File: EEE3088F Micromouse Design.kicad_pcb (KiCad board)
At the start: 2 copper layers, 70 x 78.2 mm, 39 parts, among them J1 Conn_02x16_Odd_Even, J2 Conn_01x02, J3 TYPE-C-31-M-12, SW1 SW_SPDT, U1 INA219AxD, U2 XL1509-3.3, U7 TPS61088RHLR, U9 CH224K

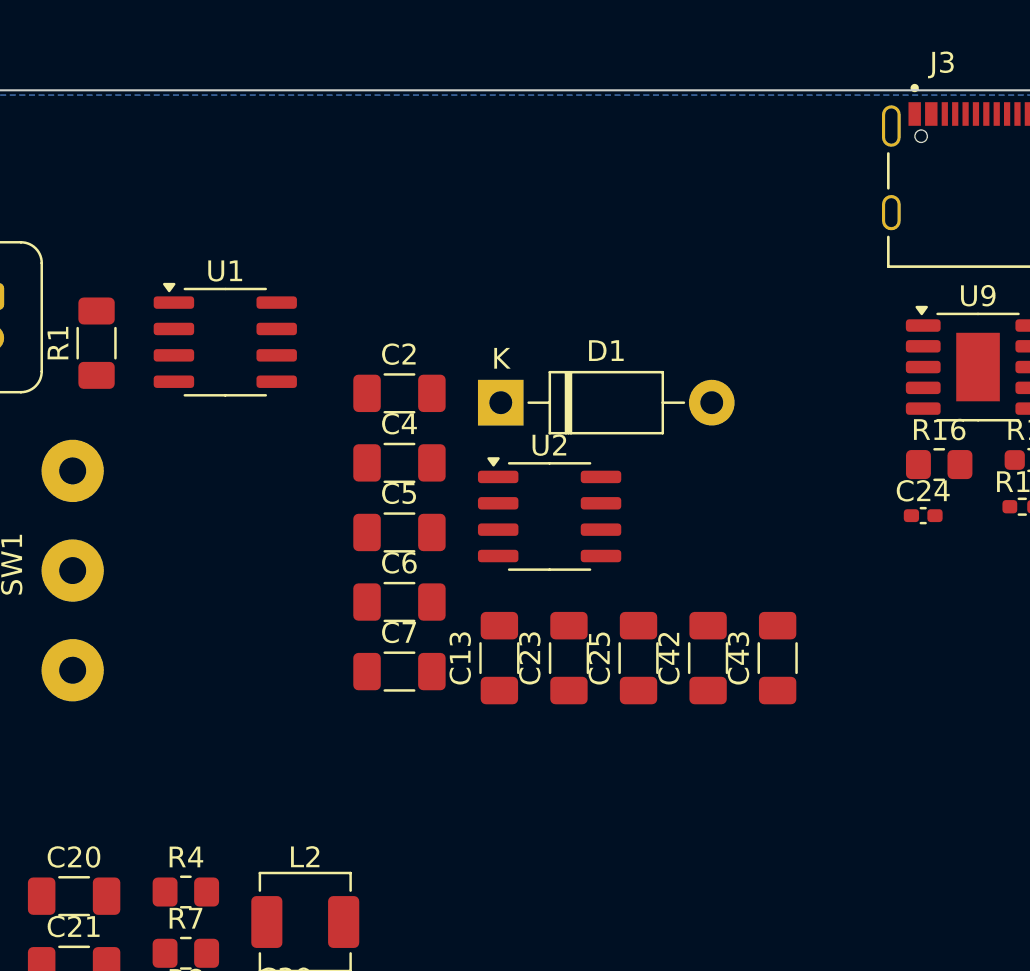
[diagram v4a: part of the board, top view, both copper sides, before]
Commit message: Added some text on the silkscreen to delimit the modules
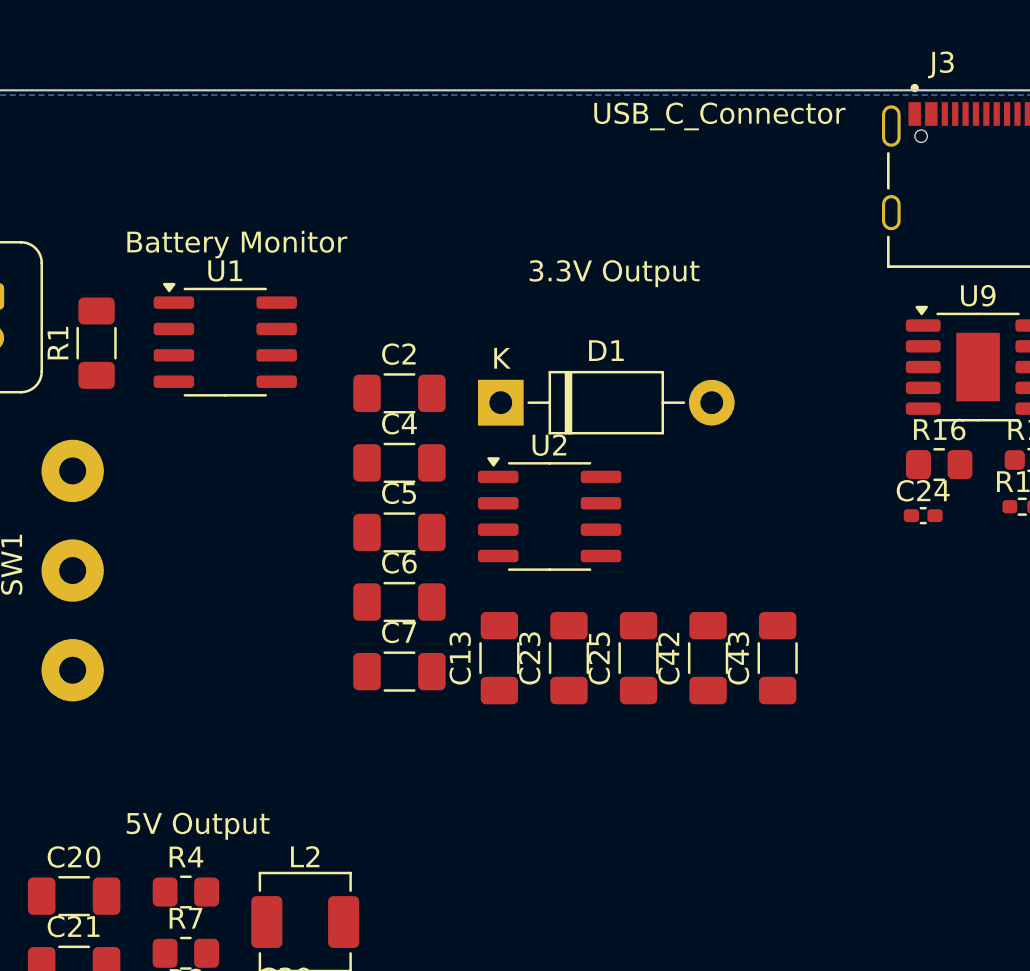
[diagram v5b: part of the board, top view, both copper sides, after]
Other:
- board text added: "3.3V Output"
- board text added: "5V Output"
- board text added: "Battery Monitor"
- board text added: "USB_C_Connector"
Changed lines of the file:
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@@
 		(layer "Edge.Cuts")
+	)
+	(gr_text "Battery Monitor"
+		(at 67 64.7 0)
+		(layer "F.SilkS")
+		(effects
+			(font
+				(size 1 1)
+				(thickness 0.15)
+			)
+			(justify left bottom)
+		)
+	)
+	(gr_text "USB_C_Connector"
+		(at 89.5 58.5 0)
+		(layer "F.SilkS")
+		(effects
+			(font
+				(size 1 1)
+				(thickness 0.15)
+			)
+			(justify left bottom)
+		)
+	)
+	(gr_text "5V Output"
+		(at 67 92.7 0)
+		(layer "F.SilkS")
+		(effects
+			(font
+				(size 1 1)
+				(thickness 0.15)
+			)
+			(justify left bottom)
+		)
+	)
+	(gr_text "3.3V Output\n\n"
+		(at 86.4 67.7 0)
+		(layer "F.SilkS")
+		(effects
+			(font
+				(size 1 1)
+				(thickness 0.15)
+			)
+			(justify left bottom)
+		)
 	)
 	(zone

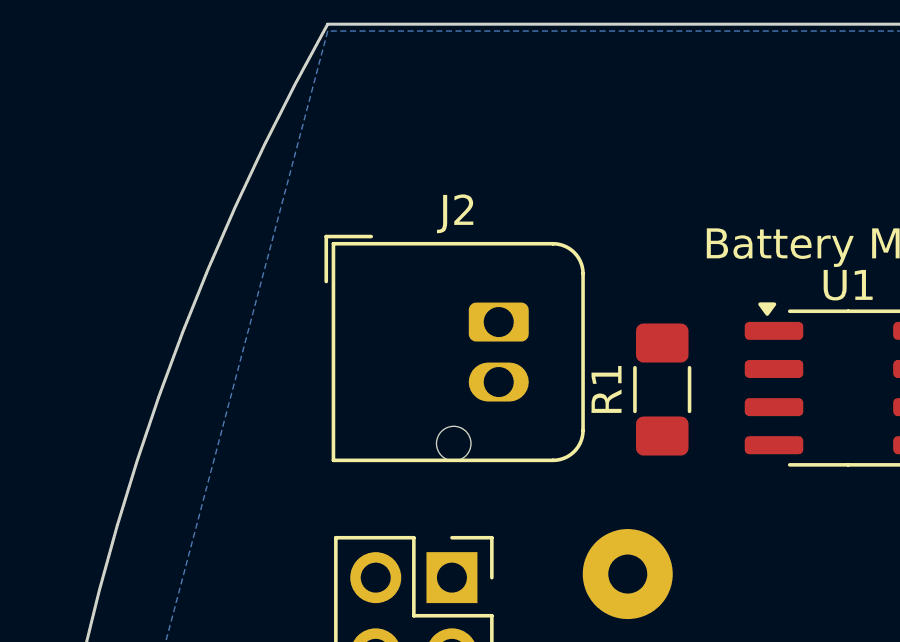
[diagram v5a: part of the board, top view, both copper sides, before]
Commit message: Found the correct Battery connector
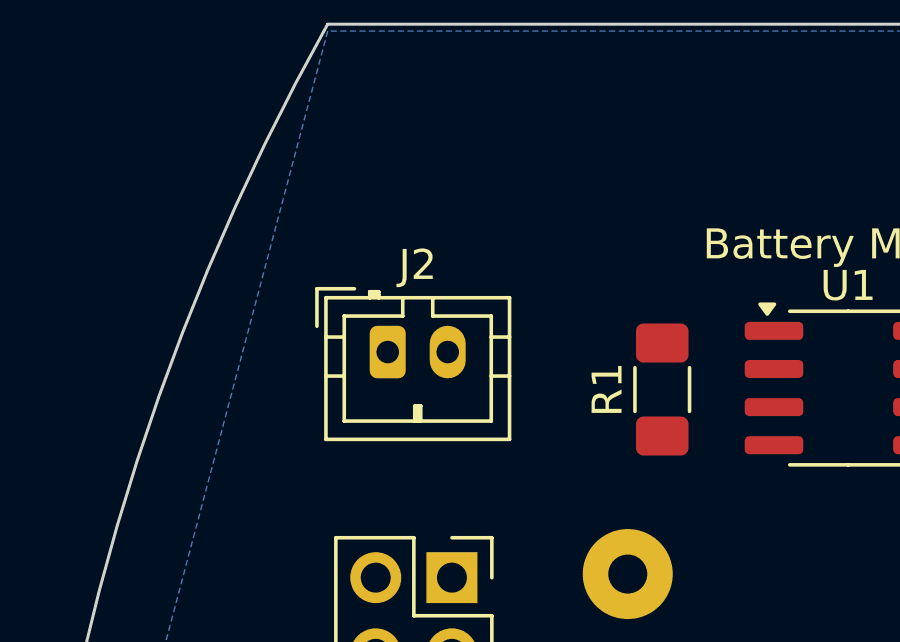
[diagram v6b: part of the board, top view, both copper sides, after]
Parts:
- J2: footprint Connector_JST:JST_JWPF_B02B-JWPF-SK-R_1x02_P2.00mm_Vertical -> Connector_JST:JST_PH_B2B-PH-K_1x02_P2.00mm_Vertical
- moved J2 3.83 mm to (56.5, 67.7)

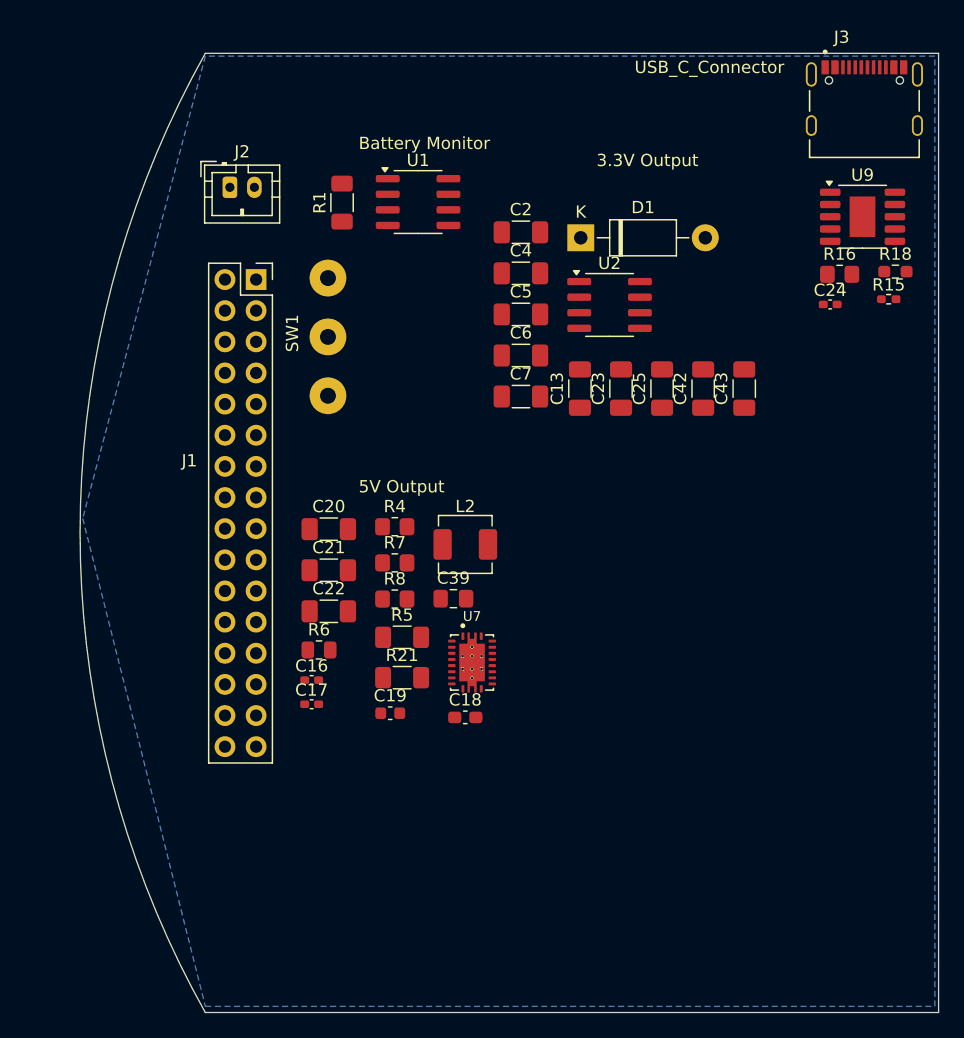
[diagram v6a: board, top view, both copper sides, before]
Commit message: Added test points and an inductor that was not populated. Added labels
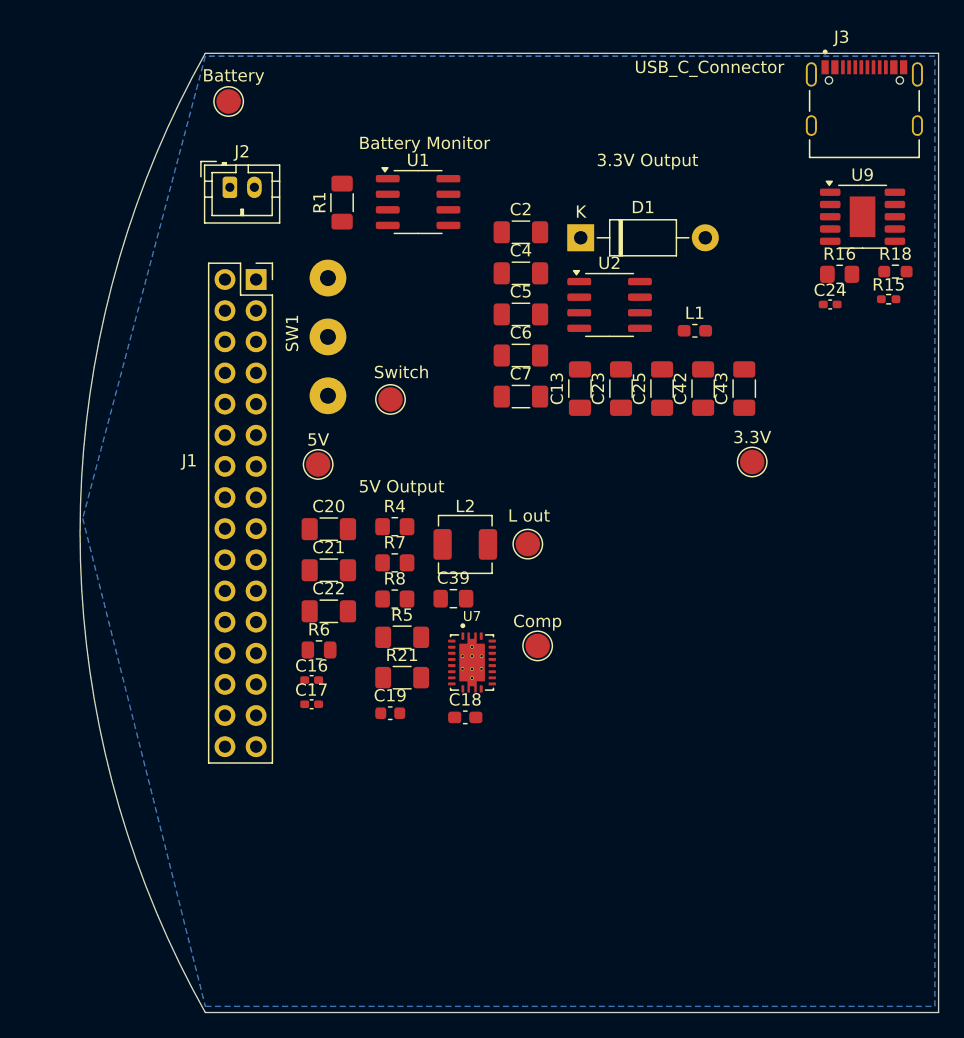
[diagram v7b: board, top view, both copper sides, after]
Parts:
- added 3.3V: TestPoint, TestPoint:TestPoint_Pad_D2.0mm, F.Cu at (99.1, 90.1)
- added 5V: TestPoint, TestPoint:TestPoint_Pad_D2.0mm, F.Cu at (63.7, 90.3)
- added Battery: TestPoint, TestPoint:TestPoint_Pad_D2.0mm, F.Cu at (56.4, 60.7)
- added Comp: TestPoint, TestPoint:TestPoint_Pad_D2.0mm, F.Cu at (81.6, 105.1)
- added L out: TestPoint, TestPoint:TestPoint_Pad_D2.0mm, F.Cu at (80.8, 96.8)
- added L1: 22uH, Inductor_SMD:L_0603_1608Metric_Pad1.05x0.95mm_HandSolder, F.Cu at (94.4, 79.4)
- added Switch: TestPoint, TestPoint:TestPoint_Pad_D2.0mm, F.Cu at (69.6, 85.0)
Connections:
- U1 pad 2: /V_Battery- -> GND

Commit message: Found a component that I had not footprinted yet. use the footprint list to check yours please
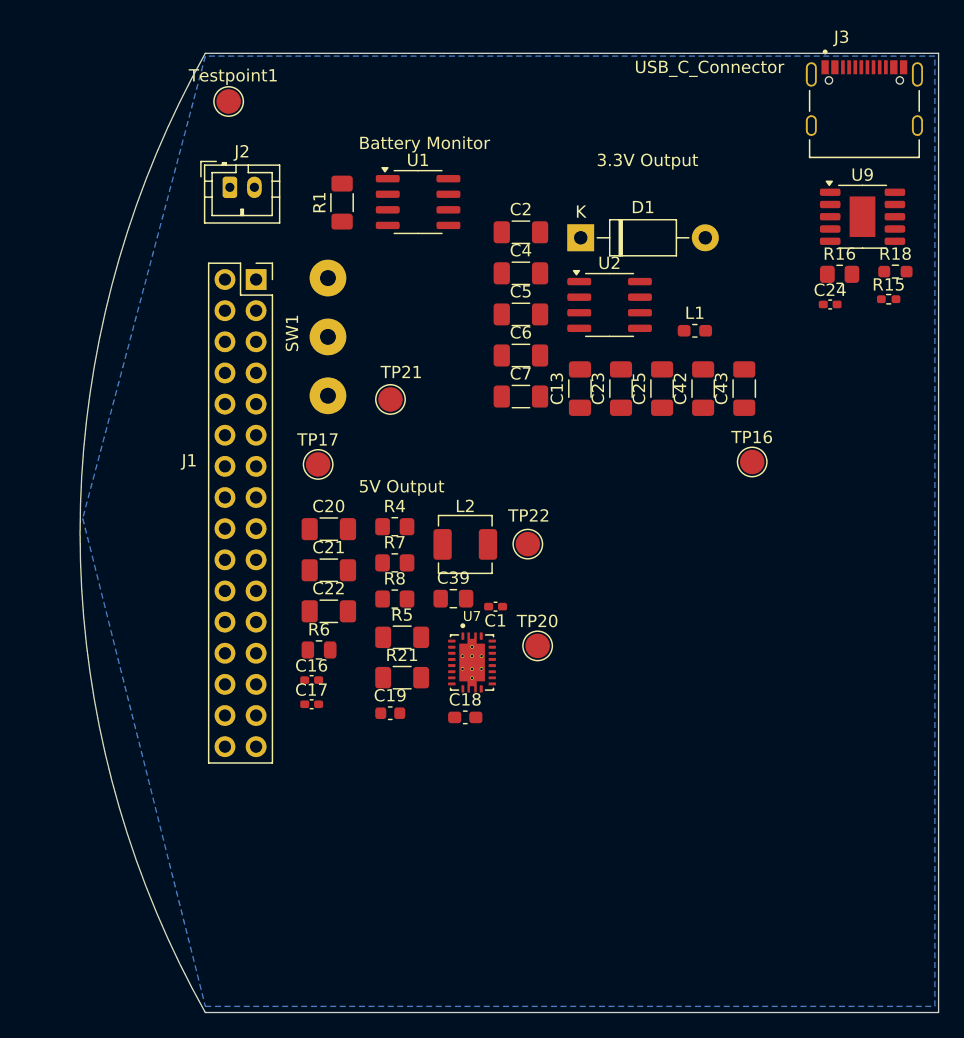
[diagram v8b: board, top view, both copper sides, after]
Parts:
- added C1: 1uF, Capacitor_SMD:C_0402_1005Metric_Pad0.74x0.62mm_HandSolder, F.Cu at (78.2, 101.9)
- TP22: renamed from L out
- renumbered 3.3V to TP16, 5V to TP17, Comp to TP20, Switch to TP21, Battery to Testpoint1
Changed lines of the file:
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@@
 		(descr "SMD pad as test Point, diameter 2.0mm")
 		(tags "test point SMD pad")
-		(property "Reference" "Battery"
+		(property "Reference" "Testpoint1"
 			(at 0.4 -2.1 0)
 			(layer "F.SilkS")
@@
 		(descr "SMD pad as test Point, diameter 2.0mm")
 		(tags "test point SMD pad")
-		(property "Reference" "Switch"
+		(property "Reference" "TP21"
 			(at 0.9 -2.2 0)
 			(layer "F.SilkS")
@@
 		(descr "SMD pad as test Point, diameter 2.0mm")
 		(tags "test point SMD pad")
-		(property "Reference" "5V"
+		(property "Reference" "TP17"
 			(at 0 -2 0)
 			(layer "F.SilkS")
@@
 			)
 		)
-		(property "LCSC" "     C17801"
+		(property "LCSC" "C17801"
 			(at 0 0 0)
 			(unlocked yes)
@@
 		)
 	)
+	(footprint "Capacitor_SMD:C_0402_1005Metric_Pad0.74x0.62mm_HandSolder"
+		(layer "F.Cu")
+		(at 78.1675 101.9 180)
+		(descr "Capacitor SMD 0402 (1005 Metric), square (rectangular) end terminal, IPC_7351 nominal with elongated pad for handsoldering. (Body size source: IPC-SM-782 page 76, https://www.pcb-3d.com/wordpress/wp-content/uploads/ipc-sm-782a_amendment_1_and_2.pdf), generated with kicad-footprint-generator")
+		(tags "capacitor handsolder")
+		(property "Reference" "C1"
+			(at 0 -1.16 0)
+			(layer "F.SilkS")
+			(effects
+				(font
+					(size 1 1)
+					(thickness 0.15)
+				)
+			)
+		)
+		(property "Value" "1uF"
+			(at 0 1.16 0)
+			(layer "F.Fab")
+			(effects
+				(font
+					(size 1 1)
+					(thickness 0.15)
+				)
+			)
+		)
+		(property "Datasheet" ""
+			(at 0 0 180)
+			(unlocked yes)
+			(layer "F.Fab")
+			(hide yes)
+			(effects
+				(font
+					(size 1.27 1.27)
+					(thickness 0.15)
+				)
+			)
+		)
+		(property "Description" "Unpolarized capacitor, small symbol"
+			(at 0 0 180)
+			(unlocked yes)
+			(layer "F.Fab")
+			(hide yes)
+			(effects
+				(font
+					(size 1.27 1.27)
+					(thickness 0.15)
+				)
+			)
+		)
+		(property "LCSC" "C52923"
+			(at 0 0 180)
+			(unlocked yes)
+			(layer "F.Fab")
+			(hide yes)
+			(effects
+				(font
+					(size 1 1)
+					(thickness 0.15)
+				)
+			)
+		)
+		(property ki_fp_filters "C_*")
+		(sheetname "/")
+		(sheetfile "EEE3088F Micromouse Design.kicad_sch")
+		(attr smd)
+		(fp_line
+			(start -0.115835 0.36)
+			(end 0.115835 0.36)
+			(stroke
+				(width 0.12)
+				(type solid)
+			)
+			(layer "F.SilkS")
+		)
+		(fp_line
+			(start -0.115835 -0.36)
+			(end 0.115835 -0.36)
+			(stroke
+				(width 0.12)
+				(type solid)
+			)
+			(layer "F.SilkS")
+		)
+		(fp_line
+			(start 1.08 0.46)
+			(end -1.08 0.46)
+			(stroke
+				(width 0.05)
+				(type solid)
+			)
+			(layer "F.CrtYd")
+		)
+		(fp_line
+			(start 1.08 -0.46)
+			(end 1.08 0.46)
+			(stroke
+				(width 0.05)
+				(type solid)
+			)
+			(layer "F.CrtYd")
+		)
+		(fp_line
+			(start -1.08 0.46)
+			(end -1.08 -0.46)
+			(stroke
+				(width 0.05)
+				(type solid)
+			)
+			(layer "F.CrtYd")
+		)
+		(fp_line
+			(start -1.08 -0.46)
+			(end 1.08 -0.46)
+			(stroke
+				(width 0.05)
+				(type solid)
+			)
+			(layer "F.CrtYd")
+		)
+		(fp_line
+			(start 0.5 0.25)
+			(end -0.5 0.25)
+			(stroke
+				(width 0.1)
+				(type solid)
+			)
+			(layer "F.Fab")
+		)
+		(fp_line
+			(start 0.5 -0.25)
+			(end 0.5 0.25)
+			(stroke
+				(width 0.1)
+				(type solid)
+			)
+			(layer "F.Fab")
+		)
+		(fp_line
+			(start -0.5 0.25)
+			(end -0.5 -0.25)
+			(stroke
+				(width 0.1)
+				(type solid)
+			)
+			(layer "F.Fab")
+		)
+		(fp_line
+			(start -0.5 -0.25)
+			(end 0.5 -0.25)
+			(stroke
+				(width 0.1)
+				(type solid)
+			)
+			(layer "F.Fab")
+		)
+		(fp_text user "${REFERENCE}"
+			(at 0 0 0)
+			(layer "F.Fab")
+			(effects
+				(font
+					(size 0.25 0.25)
+					(thickness 0.04)
+				)
+			)
+		)
+		(pad "1" smd roundrect
+			(at -0.5675 0 180)
+			(size 0.735 0.62)
+			(layers "F.Cu" "F.Mask" "F.Paste")
+			(roundrect_rratio 0.25)
+			(net 1 "/5V Out")
+			(pintype "passive")
+		)
+		(pad "2" smd roundrect
+			(at 0.5675 0 180)
+			(size 0.735 0.62)
+			(layers "F.Cu" "F.Mask" "F.Paste")
+			(roundrect_rratio 0.25)
+			(net 28 "GND")
+			(pintype "passive")
+		)
+		(embedded_fonts no)
+		(model "${KICAD9_3DMODEL_DIR}/Capacitor_SMD.3dshapes/C_0402_1005Metric.wrl"
+			(offset
+				(xyz 0 0 0)
+			)
+			(scale
+				(xyz 1 1 1)
+			)
+			(rotate
+				(xyz 0 0 0)
+			)
+		)
+	)
 	(footprint "Capacitor_SMD:C_1206_3216Metric_Pad1.33x1.80mm_HandSolder"
 		(layer "F.Cu")
@@
 		(descr "SMD pad as test Point, diameter 2.0mm")
 		(tags "test point SMD pad")
-		(property "Reference" "3.3V"
+		(property "Reference" "TP16"
 			(at 0 -1.998 0)
 			(layer "F.SilkS")
@@
 		(descr "SMD pad as test Point, diameter 2.0mm")
 		(tags "test point SMD pad")
-		(property "Reference" "L out"
+		(property "Reference" "TP22"
 			(at 0.1 -2.3 0)
 			(layer "F.SilkS")
@@
 		(descr "SMD pad as test Point, diameter 2.0mm")
 		(tags "test point SMD pad")
-		(property "Reference" "Comp"
+		(property "Reference" "TP20"
 			(at 0 -1.998 0)
 			(layer "F.SilkS")
